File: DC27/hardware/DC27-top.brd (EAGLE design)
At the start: 102.4 x 117.6 mm, 61 parts

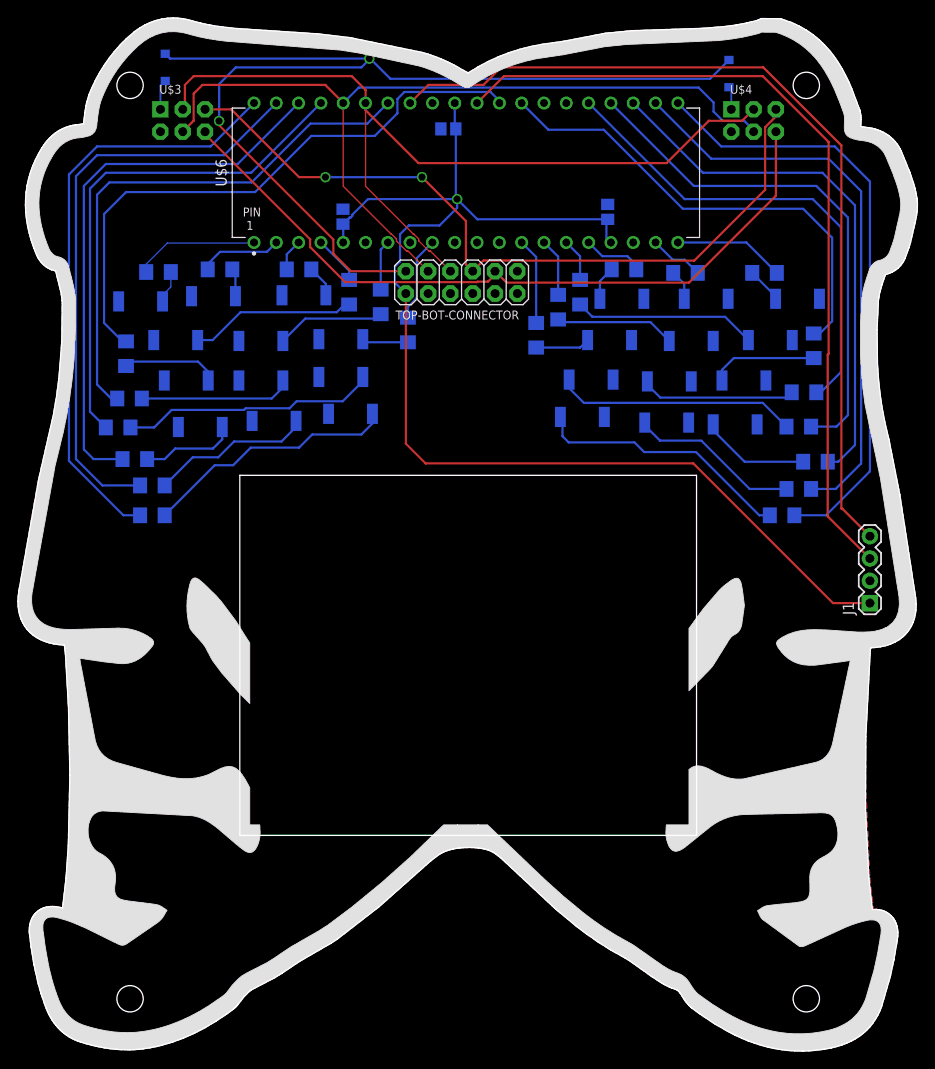
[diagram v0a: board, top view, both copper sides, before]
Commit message: Enable line of pwr switch is now what powers vbat on top board, so if you turnoff the badge top the top and the bottom board are off.  :) Increased top board caps to 1206 from 0805
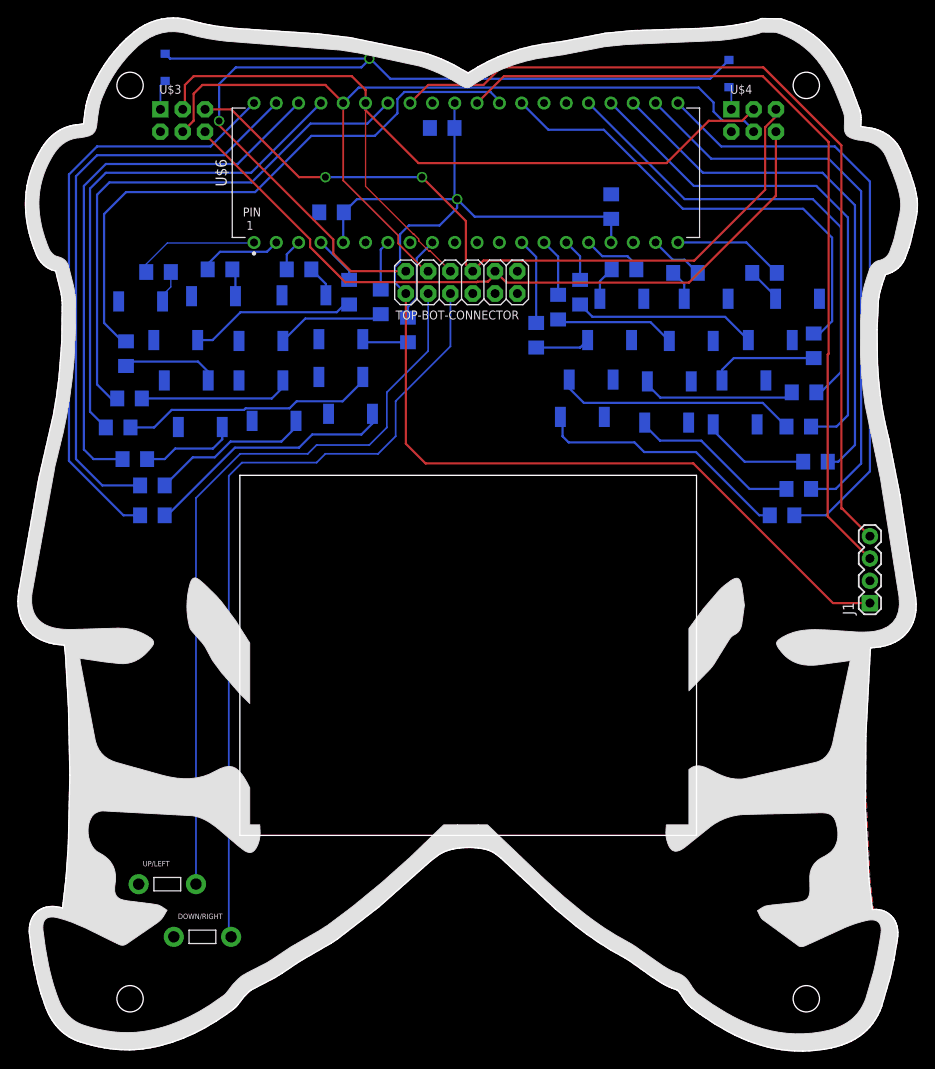
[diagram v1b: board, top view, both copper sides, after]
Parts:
- added DOWN/RIGHT, UP/LEFT: SWITCH_TACTILETACTILE-2PIN-NARROW, switches:TACTILE-2PIN-NARROW
- C1, C2, C3: device passives:C0805 -> passives:C1206
- moved C3 1.39 mm to (35.7, 95.5), turned to 180 degrees
- moved C1 0.72 mm to (67.5, 96.1)
- moved C2 0.71 mm to (48.3, 105.1)
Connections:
- new net SVN: TOP-BOT-CONNECTOR.3, UP/LEFT.P$1
- new net SVP: DOWN/RIGHT.P$1, TOP-BOT-CONNECTOR.5
- net GND: now also DOWN/RIGHT.P$2, UP/LEFT.P$2
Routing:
- net SVP: track 0.00 -> 92.3 mm
- net SVN: track 0.00 -> 86.2 mm
- net VBAT: track 142.2 -> 142.9 mm

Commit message: cleaned up silk screen top board
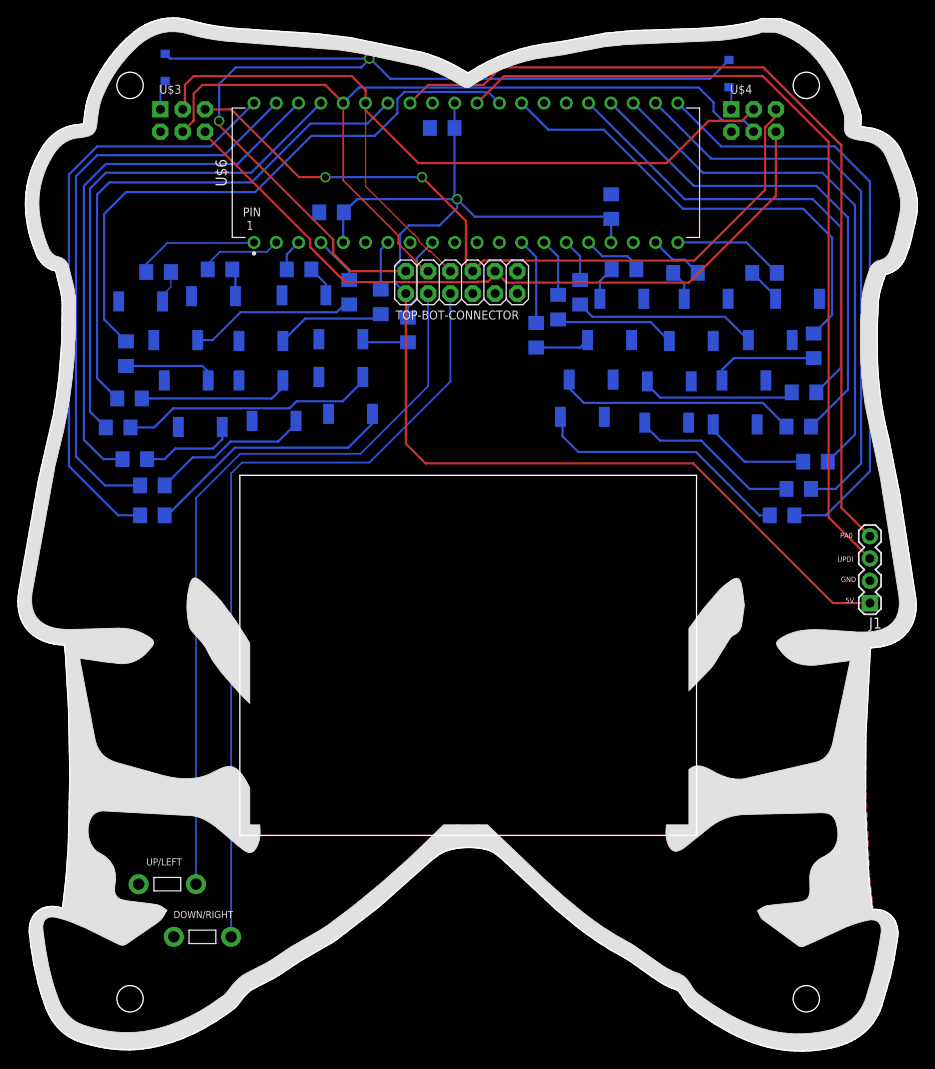
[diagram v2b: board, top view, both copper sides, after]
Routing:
- net N$46: track 59.6 -> 57.9 mm
- net N$32: track 19.2 -> 18.2 mm
- net N$47: track 61.3 -> 60.6 mm
- net N$7: track 63.2 -> 62.6 mm
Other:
- board text added: "5V"
- board text added: "GND"
- board text added: "PA0"
- board text added: "UPDI"

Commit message: added cmdc0dez puzzle
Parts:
- moved R7 2.30 mm to (44.4, 79.8)
- moved R8 0.64 mm to (40.9, 85.8)
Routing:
- net N$4: track 9.72 -> 12.0 mm
- net N$9: track 5.29 -> 6.24 mm
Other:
- board text added: "1 15 18 14 9 4 3 11 19"
- board text added: "1929"
- board text added: "B1"
- board text added: "B2"
- board text added: "IO1"
- board text added: "IO2"
- board text added: "SCL"
- board text added: "SDA"
- board text added: "Solve my puzzle"
- board text added: "VBAT"
- board text added: "VCC"
- board text added: "khtrm://cxp.ac/2CsCuG5"

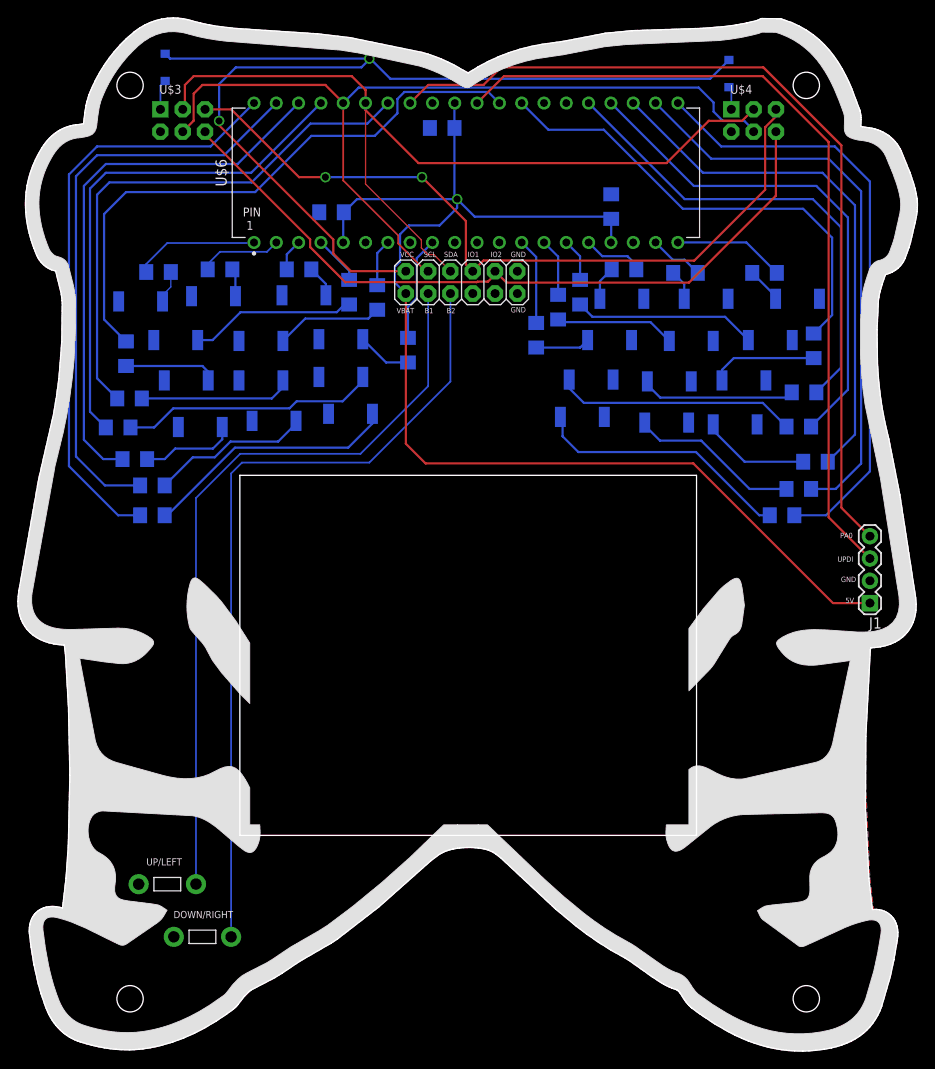
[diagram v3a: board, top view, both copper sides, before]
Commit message: Fixed the darknet logo, and made resistors pretty
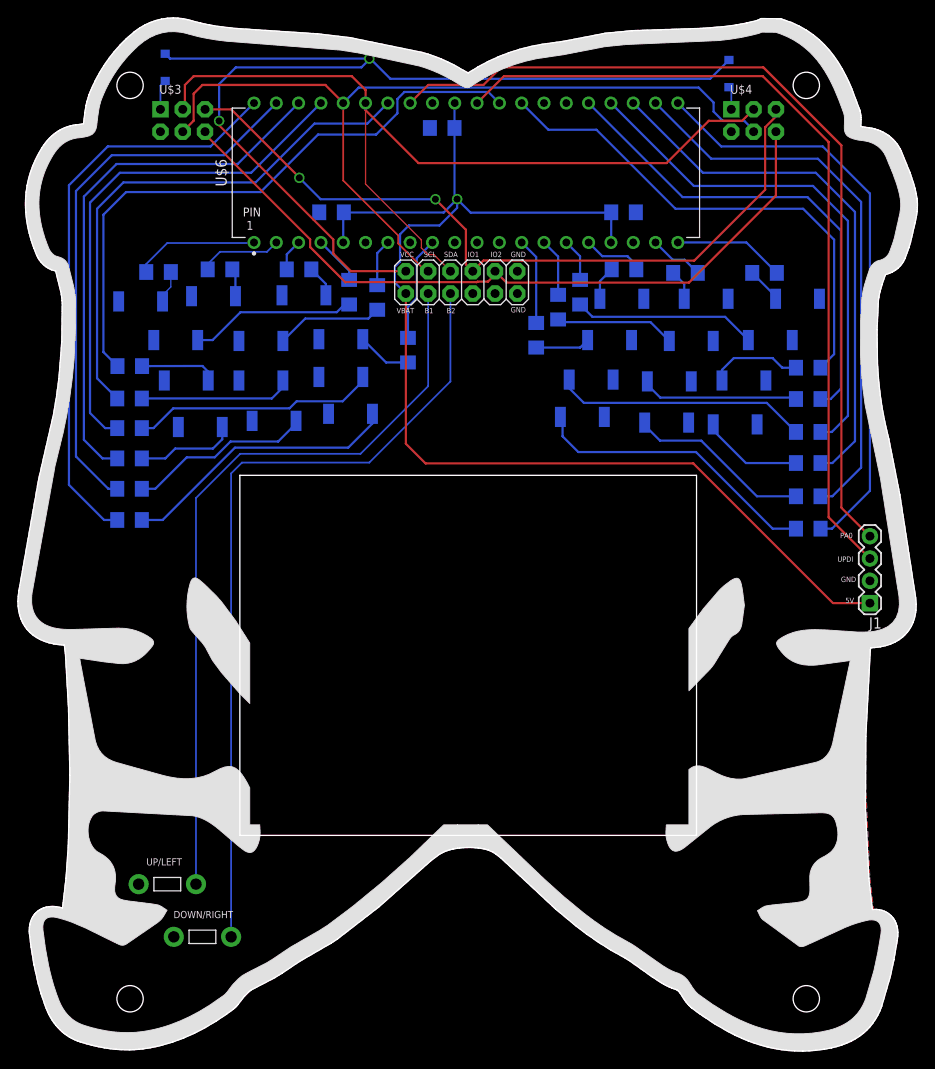
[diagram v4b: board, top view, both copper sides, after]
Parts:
- U$5: value DN_LOGO -> DN_LOGODC26; device logos:DN_LOGO_LONG_SILK -> darknet_parts_library:DN_LOGO_DC26
- moved R24 3.35 mm to (90.0, 59.5)
- moved R1 2.65 mm to (12.7, 60.5)
- moved R2 2.63 mm to (12.7, 64.0)
- moved R19 2.57 mm to (90.0, 77.8), turned to 180 degrees
- moved C1 1.55 mm to (68.9, 95.5), turned to 0 degrees
- moved R6 1.48 mm to (12.7, 78.0), turned to 0 degrees
- moved R23 1.37 mm to (90.0, 63.2)
- moved R4 1.30 mm to (12.7, 70.9)
- moved R21 1.24 mm to (90.0, 70.5)
- moved R20 0.90 mm to (90.0, 74.2)
- moved R22 0.83 mm to (90.0, 66.9)
- moved R3 0.60 mm to (12.7, 67.5)
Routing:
- net N$44: track 53.5 -> 57.2 mm
- net N$35: track 29.6 -> 33.2 mm
- net N$6: track 66.8 -> 63.4 mm
- net N$31: track 29.1 -> 31.9 mm
- net N$32: track 18.2 -> 20.9 mm
- net N$27: track 67.8 -> 70.3 mm
- net N$49: track 69.2 -> 67.4 mm
- net N$5: track 68.1 -> 66.2 mm
- net N$28: track 10.6 -> 8.80 mm
- net N$41: track 12.2 -> 10.6 mm
- net N$39: track 19.4 -> 20.9 mm
- net N$7: track 62.6 -> 61.2 mm
- net N$42: track 27.5 -> 28.9 mm
- net N$29: track 29.1 -> 27.9 mm
- net N$48: track 65.5 -> 64.3 mm
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
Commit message: fixed an airwire, changed diodes to through hole
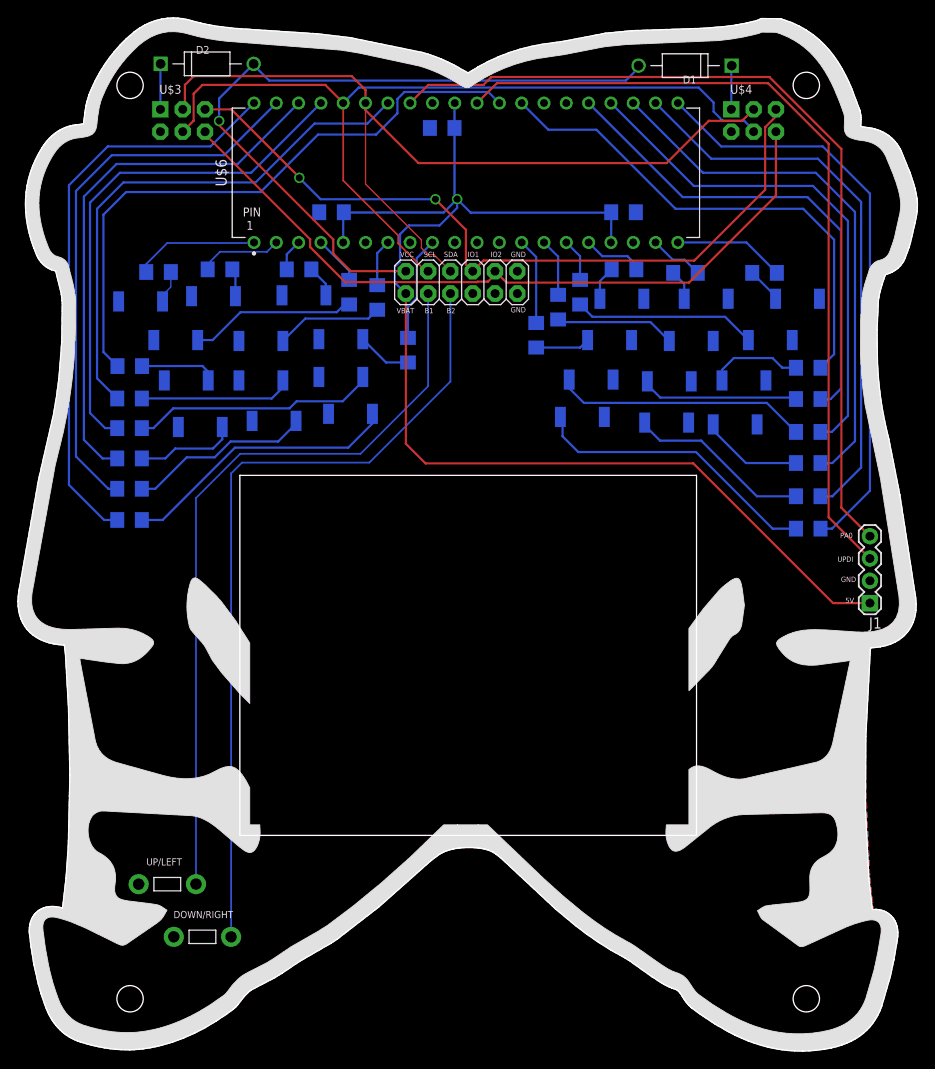
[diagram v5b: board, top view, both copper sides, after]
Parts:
- D1, D2: value DIODE-SCHOTTKYSOD-123FL -> DIODE-SCHOTTKYDIOAD-TH; device passives:SOD-123FL -> passives:DIOAD1060W80L520D270
- moved D1 5.08 mm to (76.0, 112.2), flipped to the top, turned to 180 degrees
- moved D2 4.80 mm to (21.5, 112.4), flipped to the top, turned to 0 degrees
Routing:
- net VCC: track 118.4 -> 83.2 mm, vias 2 -> 1
- net N$26: track 2.63 -> 5.00 mm
- net N$25: track 3.45 -> 5.19 mm
- net PA0: track 100.3 -> 99.2 mm
- net UPDI: track 93.8 -> 93.0 mm
